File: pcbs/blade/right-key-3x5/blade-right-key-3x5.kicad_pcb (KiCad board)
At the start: 2 copper layers, 133 x 90.1 mm, 105 parts, among them J1 expantion1, J11 Conn_01x04_Female, J12 USB-C USB 2.0 MC-372, J16 Conn_01x03_Male, J3 Conn_01x07, J5 Conn_01x05, J9 Conn_Display_general, Q1 AO3407, Q2 AO3407, SW1 SW_PUSH-kbd, SW10 SW_PUSH-kbd, SW11 SW_PUSH-kbd, SW12 SW_PUSH-kbd, SW14 SW_PUSH-kbd, SW15 SW_PUSH-kbd, SW16 SW_PUSH-kbd, SW17 SW_PUSH-kbd, SW18 SW_PUSH-kbd, SW2 SW_PUSH-kbd, SW20 SW_PUSH-kbd, SW3 SW_PUSH-kbd, SW4 SW_PUSH-kbd, SW5 SW_PUSH-kbd, SW6 SW_PUSH-kbd, SW7 SW_PUSH-kbd, SW8 SW_PUSH-kbd, SW9 SW_PUSH-kbd, U1 E73-2G4M08S1C, U2 SRV05-4, U3 XC6220B331MR-G, U4 MAX17048, U5 TP4054, U6 PMW3610, U7 MCP1700-1802E-TT, U8 CAP1203, X1 32.768 kHz

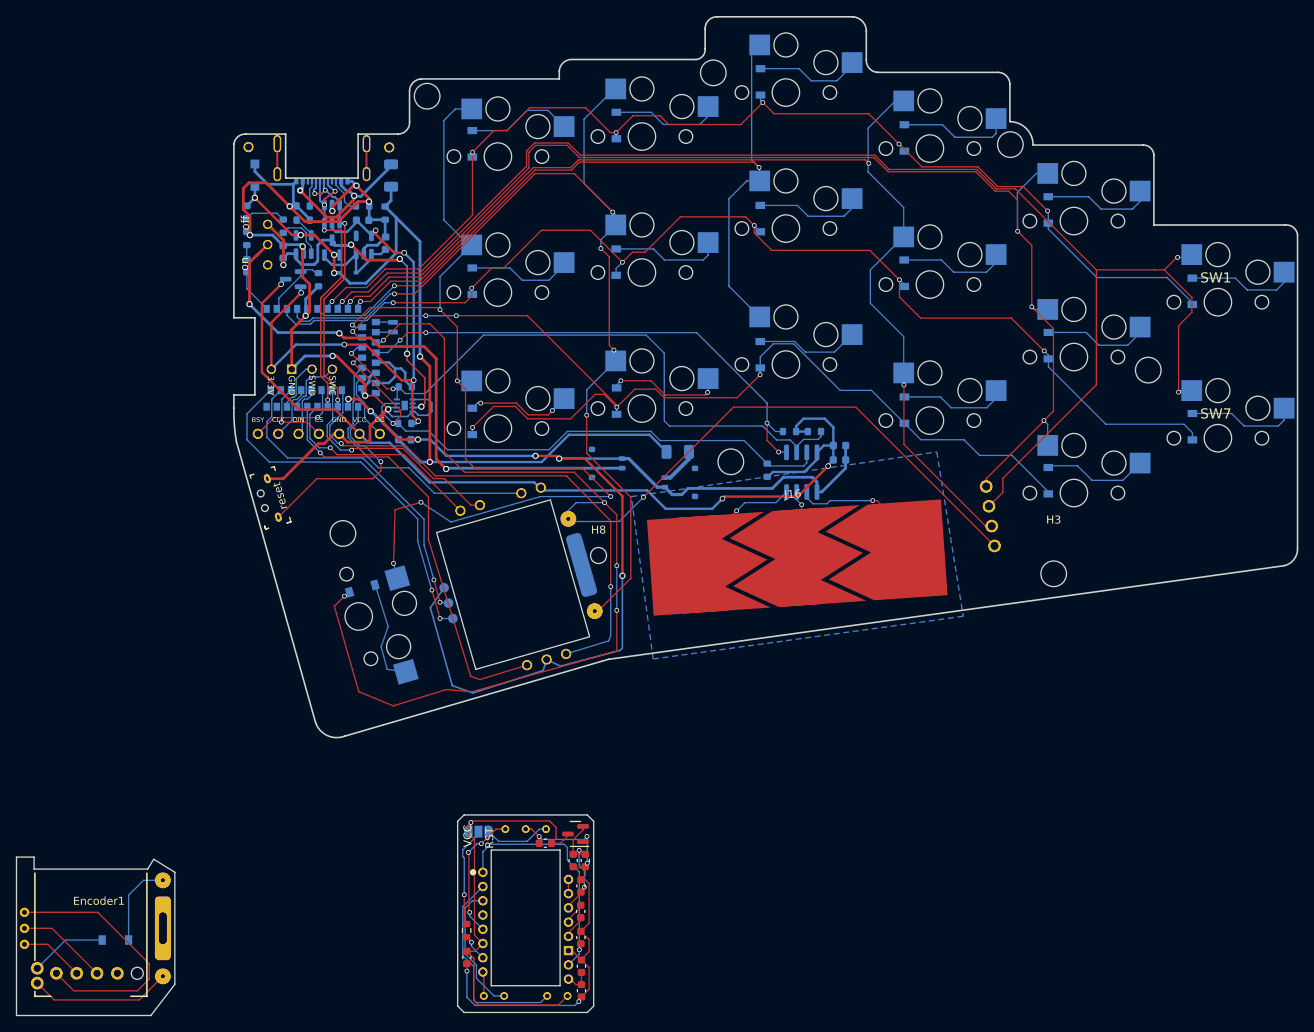
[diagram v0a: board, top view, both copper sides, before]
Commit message: add blade right with only keys (3x5)
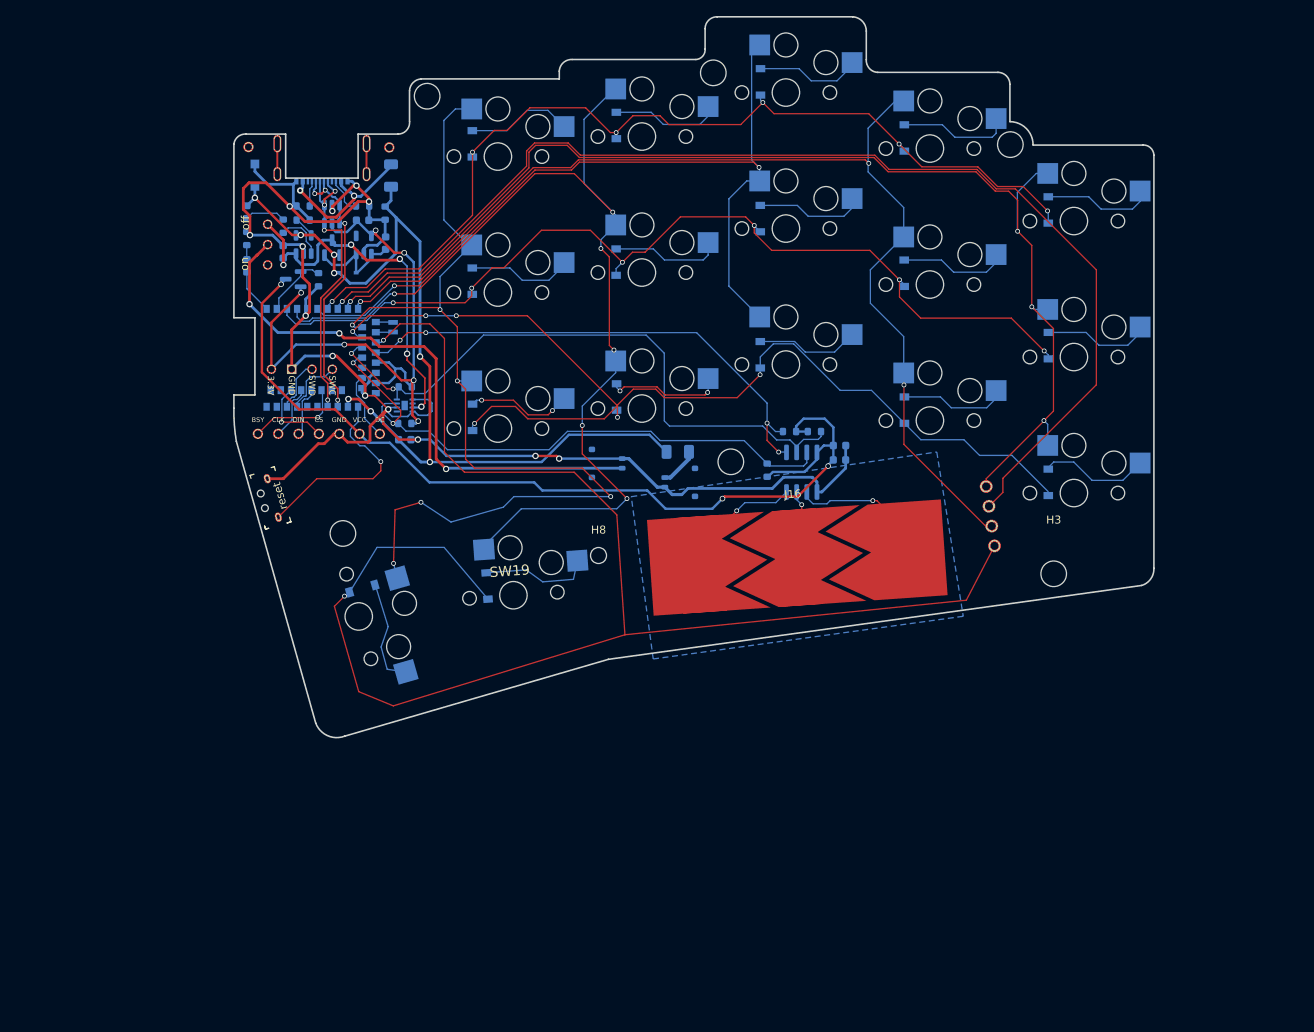
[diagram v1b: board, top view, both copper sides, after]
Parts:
- removed C10, C9: 1u, Capacitor_SMD:C_0603_1608Metric
- removed C11, C6: 100n, Capacitor_SMD:C_0603_1608Metric
- removed C12: 10u (X7R), Capacitor_SMD:C_0603_1608Metric
- removed C13: 10n (X7R), Capacitor_SMD:C_0603_1608Metric
- removed C5: 10n, Capacitor_SMD:C_0603_1608Metric
- removed C7: 3.3u/16V, Capacitor_SMD:C_0603_1608Metric
- removed C8: 100n (X7R), Capacitor_SMD:C_0603_1608Metric
- removed D1, D21, D7: 1N4148W, mylib:Diode
- removed Encoder1: RotaryEncoder, mylib:Panasonic_EVQWGD001_Latest
- removed H4: MountingHole, MountingHole:MountingHole_3.2mm_M3_DIN965
- removed J3: Conn_01x07, mylib:PMW3610-Ref-Male
- removed J5: Conn_01x05, mylib:Panasonic_EVQWGD001_Ref_Male
- removed JP1: SolderJumper_3_Open, Jumper:SolderJumper-3_P1.3mm_Open_RoundedPad1.0x1.5mm_NumberLabels
- removed R13: 2M, Resistor_SMD:R_0603_1608Metric
- removed Ref1: Conn_01x05, mylib:Panasonic_EVQWGD001_Ref
- removed Ref2: Conn_1x07, mylib:PMW3610-Ref
- removed SW1, SW7: SW_PUSH-kbd, mylib:Kailh_Choc_Hotplug
- removed U6: PMW3610, mylib:PMW3610
- removed U7: MCP1700-1802E-TT, Package_TO_SOT_SMD:SOT-23
- added D19: 1N4148W, mylib:Diode, B.Cu at (108.5, 107.2)
- added SW19: SW_PUSH-kbd, mylib:Kailh_Choc_Hotplug, F.Cu at (111.8, 108.4)
- moved D18 0.51 mm to (106.7, 86.1)
- moved D17 0.51 mm to (124.7, 83.6)
- moved D14 0.21 mm to (178.7, 94.3)
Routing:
- net /mcu/0.15/hi: track 66.3 -> 0.00 mm, vias 2 -> 0
- net GND: track 276.6 -> 211.1 mm, vias 14 -> 13
- net /trackball/GND: track 55.4 -> 0.00 mm, vias 5 -> 0
- net /trackball/3.3V: track 54.4 -> 0.00 mm, vias 1 -> 0
- net /mcu/0.24: track 52.8 -> 0.00 mm, vias 1 -> 0
- net /mcu/1.06: track 47.3 -> 0.00 mm, vias 2 -> 0
- net /mcu/1.04: track 42.2 -> 0.00 mm, vias 2 -> 0
- net /mcu/0.12/hi: track 34.0 -> 0.00 mm
- net /encoder/GND: track 33.3 -> 0.00 mm
- net /keyboard/COL_1: track 177.9 -> 146.1 mm, vias 3 -> 1
- net Net-(C5-Pad1): track 30.4 -> 0.00 mm, vias 1 -> 0
- net /mcu/0.17/hi: track 28.8 -> 0.00 mm, vias 1 -> 0
- net /mcu/0.13: track 26.9 -> 0.00 mm, vias 1 -> 0
- net /trackball/SDIO: track 25.5 -> 0.00 mm
- net /keyboard/ROW_2: track 143.2 -> 119.9 mm
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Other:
- board size 133 x 90.1 mm -> 115 x 90.1 mm
- board text removed: "RST"
- board text removed: "VCC"
